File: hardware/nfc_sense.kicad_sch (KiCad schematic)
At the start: 24 parts, among them U1 TMP117AIDRVR, U2 RF430CL330HIRGTR‎, U3 ATtiny1626-MFR

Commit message: desc + new TP
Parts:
- added TP5: TestPoint, TestPoint:TestPoint_Pad_D1.0mm, symbol Connector:TestPoint
- U1: footprint unsurv_offline_pcb_footprints:TMP117 WSON-6-1EP_2x2mm_P0.65mm -> unsurv_offline_pcb_footprints:TMP117 WSON-6-1EP_2x2mm_P0.65mm_no_pad_paste
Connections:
- net ANT2: now also TP5.1
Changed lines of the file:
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@@
+		)
+	)
+	(global_label "ANT2"
+		(shape input)
+		(at 266.7 105.41 270)
+		(fields_autoplaced yes)
+		(effects
+			(font
+				(size 1.27 1.27)
+			)
+			(justify right)
+		)
+		(property "Intersheetrefs" "${INTERSHEET_REFS}"
+			(at 266.7 112.9914 90)
+			(effects
+				(font
+					(size 1.27 1.27)
+				)
+				(justify right)
+				(hide yes)
+			)
 		)
 	)
@@
 			)
 		)
-		(property "Footprint" "unsurv_offline_pcb_footprints:TMP117 WSON-6-1EP_2x2mm_P0.65mm"
+		(property "Footprint" "unsurv_offline_pcb_footprints:TMP117 WSON-6-1EP_2x2mm_P0.65mm_no_pad_paste"
 			(at 217.805 33.655 0)
 			(effects
@@
 					(unit 1)
 				)
+			)
+		)
+	)
+	(symbol
+		(lib_id "Connector:TestPoint")
+		(at 266.7 105.41 0)
+		(unit 1)
+		(exclude_from_sim no)
+		(in_bom yes)
+		(on_board yes)
+		(dnp no)
+		(fields_autoplaced yes)
+		(property "Reference" "TP5"
+			(at 268.097 101.2733 0)
+			(effects
+				(font
+					(size 1.27 1.27)
+				)
+				(justify left)
+			)
+		)
+		(property "Value" "TestPoint"
+			(at 268.097 103.8102 0)
+			(effects
+				(font
+					(size 1.27 1.27)
+				)
+				(justify left)
+			)
+		)
+		(property "Footprint" "TestPoint:TestPoint_Pad_D1.0mm"
+			(at 271.78 105.41 0)
+			(effects
+				(font
+					(size 1.27 1.27)
+				)
+				(hide yes)
+			)
+		)
+		(property "Datasheet" "~"
+			(at 271.78 105.41 0)
+			(effects
+				(font
+					(size 1.27 1.27)
+				)
+				(hide yes)
+			)
+		)
+		(property "Description" ""
+			(at 266.7 105.41 0)
+			(effects
+				(font
+					(size 1.27 1.27)
+				)
+				(hide yes)
+			)
+		)
+		(pin "1"
+		)
+		(instances
+			(project "nfc_sense"
+				(path "/c54e1377-ff88-4224-9c85-352a20bf3450"
+					(reference "TP5")
+					(unit 1)
+				)

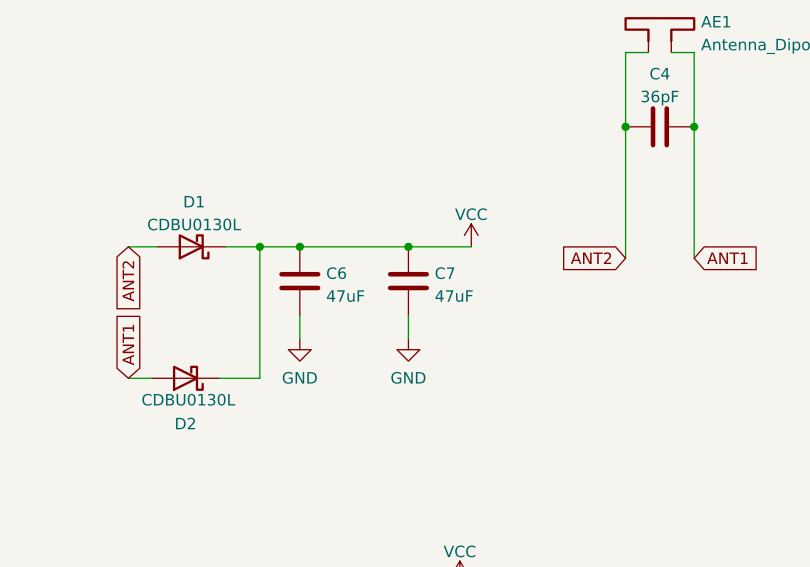
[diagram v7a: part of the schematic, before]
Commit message: change to 100uf tantalum for power siphoning
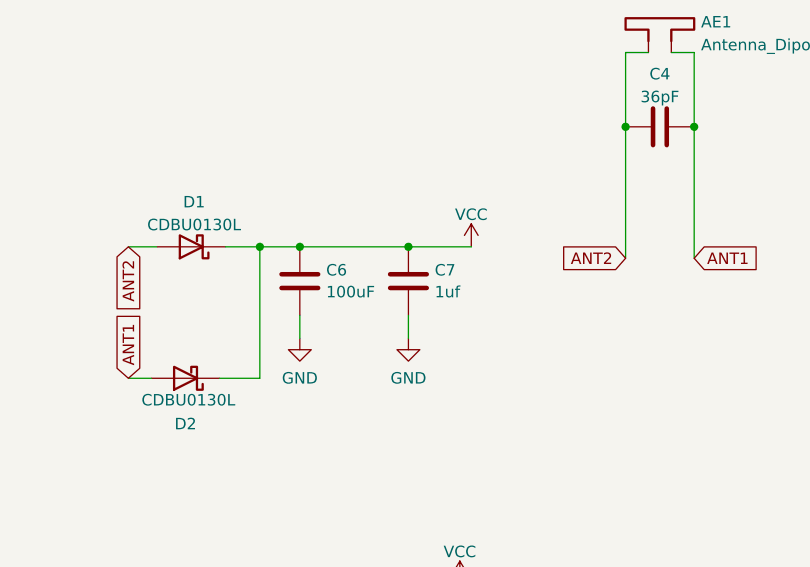
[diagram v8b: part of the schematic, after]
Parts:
- C6: value 47uF -> 100uF; MPN (none) -> 298W107X0004M2T
- C7: value 47uF -> 1uf
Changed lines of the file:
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@@
 		(fields_autoplaced yes)
 		(property "Reference" "C6"
-			(at 129.286 49.3303 0)
-			(effects
-				(font
-					(size 1.27 1.27)
-				)
-				(justify left)
-			)
-		)
-		(property "Value" "47uF"
-			(at 129.286 51.8672 0)
+			(at 129.286 48.9528 0)
+			(effects
+				(font
+					(size 1.27 1.27)
+				)
+				(justify left)
+			)
+		)
+		(property "Value" "100uF"
+			(at 129.286 51.3771 0)
 			(effects
 				(font
@@
 		)
 		(property "Description" ""
+			(at 126.365 50.165 0)
+			(effects
+				(font
+					(size 1.27 1.27)
+				)
+				(hide yes)
+			)
+		)
+		(property "MPN" "298W107X0004M2T"
 			(at 126.365 50.165 0)
 			(effects
@@
 		(fields_autoplaced yes)
 		(property "Reference" "C7"
-			(at 141.351 49.3303 0)
-			(effects
-				(font
-					(size 1.27 1.27)
-				)
-				(justify left)
-			)
-		)
-		(property "Value" "47uF"
-			(at 141.351 51.8672 0)
-			(effects
-				(font
+			(at 141.351 48.9528 0)
+			(effects
+				(font
+					(size 1.27 1.27)
+				)
+				(justify left)
+			)
+		)
+		(property "Value" "1uf"
+			(at 141.351 51.3771 0)
+			(effects
+				(font
